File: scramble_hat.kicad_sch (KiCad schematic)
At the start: 0 parts

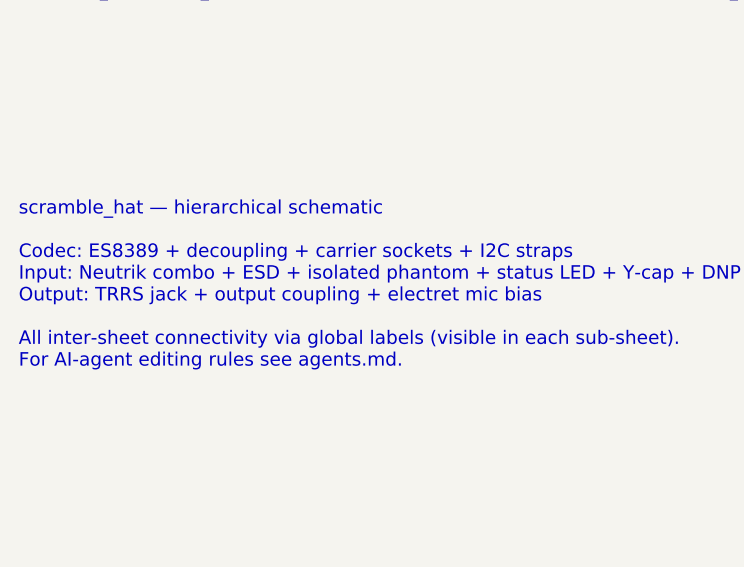
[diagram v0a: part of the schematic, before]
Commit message: fab: production prep — white/brighter status LED, C19 assembled, live BOM prices
- D8 red -> white: KT-0805W (C34499, Basic, in stock); old Kingbright
  KP-2012EC (C598272) was out of stock.
- R16 33k -> 15k, 1/4W AC0805 (C20142753) — ~2x brighter phantom-present
  LED (~3mA); resistor dissipates ~193mW at the 57V PoE max.
- C19 -> JEC JY222M2FY5VS7LE (C389727, Y2 300VAC, same 7.5mm land, in
  stock) moved onto JLCPCB THT assembly (off the hand-solder list).
- exclude_from_pos_files on J1/J2/J5 so placement/CPL leaves the
  hand-soldered parts (jacks + PoE header) to hand assembly.
- BOM: added J6, filled all resistor LCSC#s, refreshed unit prices to
  live qty-10 LCSC, corrected the D1/D2 entry.
- Regenerated gerbers/drills/BOM (csv+xlsx) with J6.
- Removed stale kicad-cli CPL — generate placement with the jlcpcb-tools
  plugin (set U1/QFN +270deg) and verify in JLCPCB preview before order.
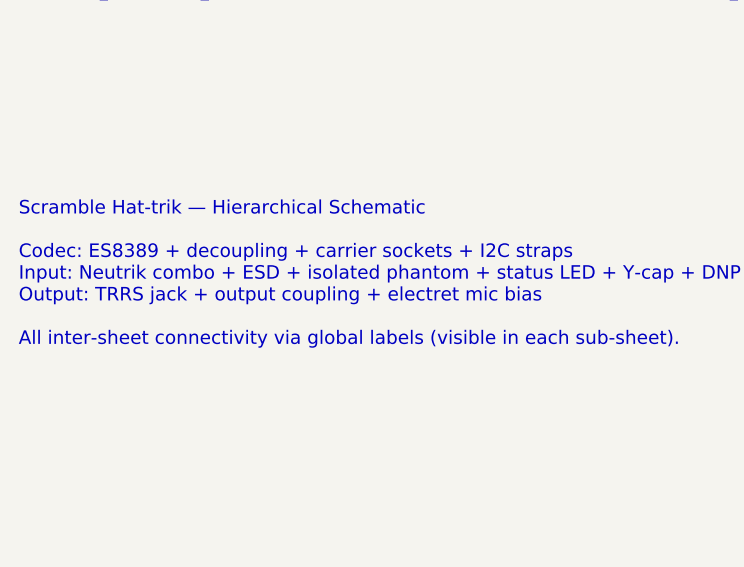
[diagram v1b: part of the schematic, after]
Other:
- note added: "Scramble Hat-trik — Hierarchical Schematic Codec: ES8389 + decoupling + carrier sockets + I2C straps Input: Neutrik combo + ESD + isolated phantom + status LED + Y-cap + DNP ground-lift Output: TRRS jack + output coupling + electret mic bias All inter-sheet connectivity via global labels (visible in each sub-sheet)."
- note removed: "scramble_hat — hierarchical schematic Codec: ES8389 + decoupling + carrier sockets + I2C straps Input: Neutrik combo + ESD + isolated phantom + status LED + Y-cap + DNP ground-lift Output: TRRS jack + output coupling + electret mic bias All inter-sheet connectivity via global labels (visible in each sub-sheet). For AI-agent editing rules see agents.md."
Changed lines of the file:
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@@
 		(comment 1 "Audio I/O hat for Waveshare ESP32-P4-ETH carrier. See agents.md for editing rules.")
 	)
-	(text "scramble_hat — hierarchical schematic\n\nCodec: ES8389 + decoupling + carrier sockets + I2C straps\nInput: Neutrik combo + ESD + isolated phantom + status LED + Y-cap + DNP ground-lift\nOutput: TRRS jack + output coupling + electret mic bias\n\nAll inter-sheet connectivity via global labels (visible in each sub-sheet).\nFor AI-agent editing rules see agents.md."
+	(text "Scramble Hat-trik — Hierarchical Schematic\n\nCodec: ES8389 + decoupling + carrier sockets + I2C straps\nInput: Neutrik combo + ESD + isolated phantom + status LED + Y-cap + DNP ground-lift\nOutput: TRRS jack + output coupling + electret mic bias\n\nAll inter-sheet connectivity via global labels (visible in each sub-sheet)."
 		(exclude_from_sim no)
 		(at 30 80 0)

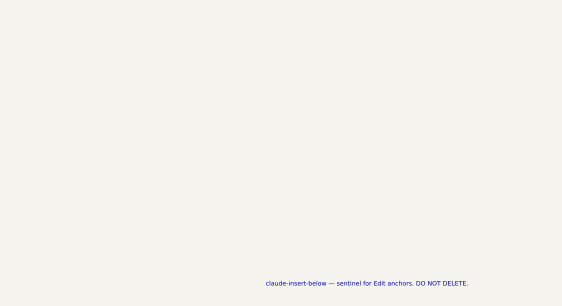
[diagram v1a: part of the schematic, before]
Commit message: sch: add datasheet links, hide Datasheet/Description fields, remove sentinel text
- Filled 38 empty component Datasheet fields with LCSC product-page links (derived from the BOM part numbers); fixed D8's stale link (Kingbright KP-2012EC -> white KT-0805W / C34499). Existing manufacturer/distributor links kept.
- Hid the Datasheet and Description fields on all 53 placed components (most were previously shown, cluttering the canvas).
- Removed the 4 leftover sentinel text annotations.
- Netlist unchanged (check_sync: in sync, 53 comps / 46 nets).
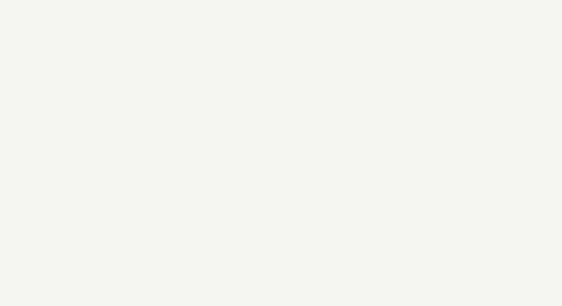
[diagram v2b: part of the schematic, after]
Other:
- note removed: "claude-insert-below — sentinel for Edit anchors. DO NOT DELETE."
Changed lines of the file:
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@@
-		)
-	)
-	(text "claude-insert-below — sentinel for Edit anchors. DO NOT DELETE."
-		(exclude_from_sim no)
-		(at 200 200 0)
-		(effects
-			(font
-				(size 0.5 0.5)
-			)
-			(justify left top)
 		)
 	)
